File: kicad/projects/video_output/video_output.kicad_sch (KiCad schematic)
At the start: 75 parts, among them J1 peripheral_addr_bus_connector, J10 DATA_BUF_DIR, J11 DATA_BUF_~{OE}, J12 LONG_PULSE, J13 ~{SHORT_PULSE}, J14 GND, J15 SAFE_CLK, J2 peripheral_aux_connector, J3 peripheral_membank_connector, J4 Conn_01x16_Socket, J5 Conn_01x16_Socket, J6 Conn_02x06_Odd_Even, J7 RAM_~{WE}, J8 video_aux, J9 Conn_01x04_Socket, U1 628128_DIP32_SSOP32, U10 74HC157, U11 74HC157, U12 74HC10, U13 74HC02, U14 74HC08, U15 74HC123, U16 74HC32, U17 74HC04, U2 628128_DIP32_SSOP32, U3 74HC245, U4 74HC245, U5 74HC245, U6 74HC245, U7 74HC574, U8 74HC245, U9 74HC574

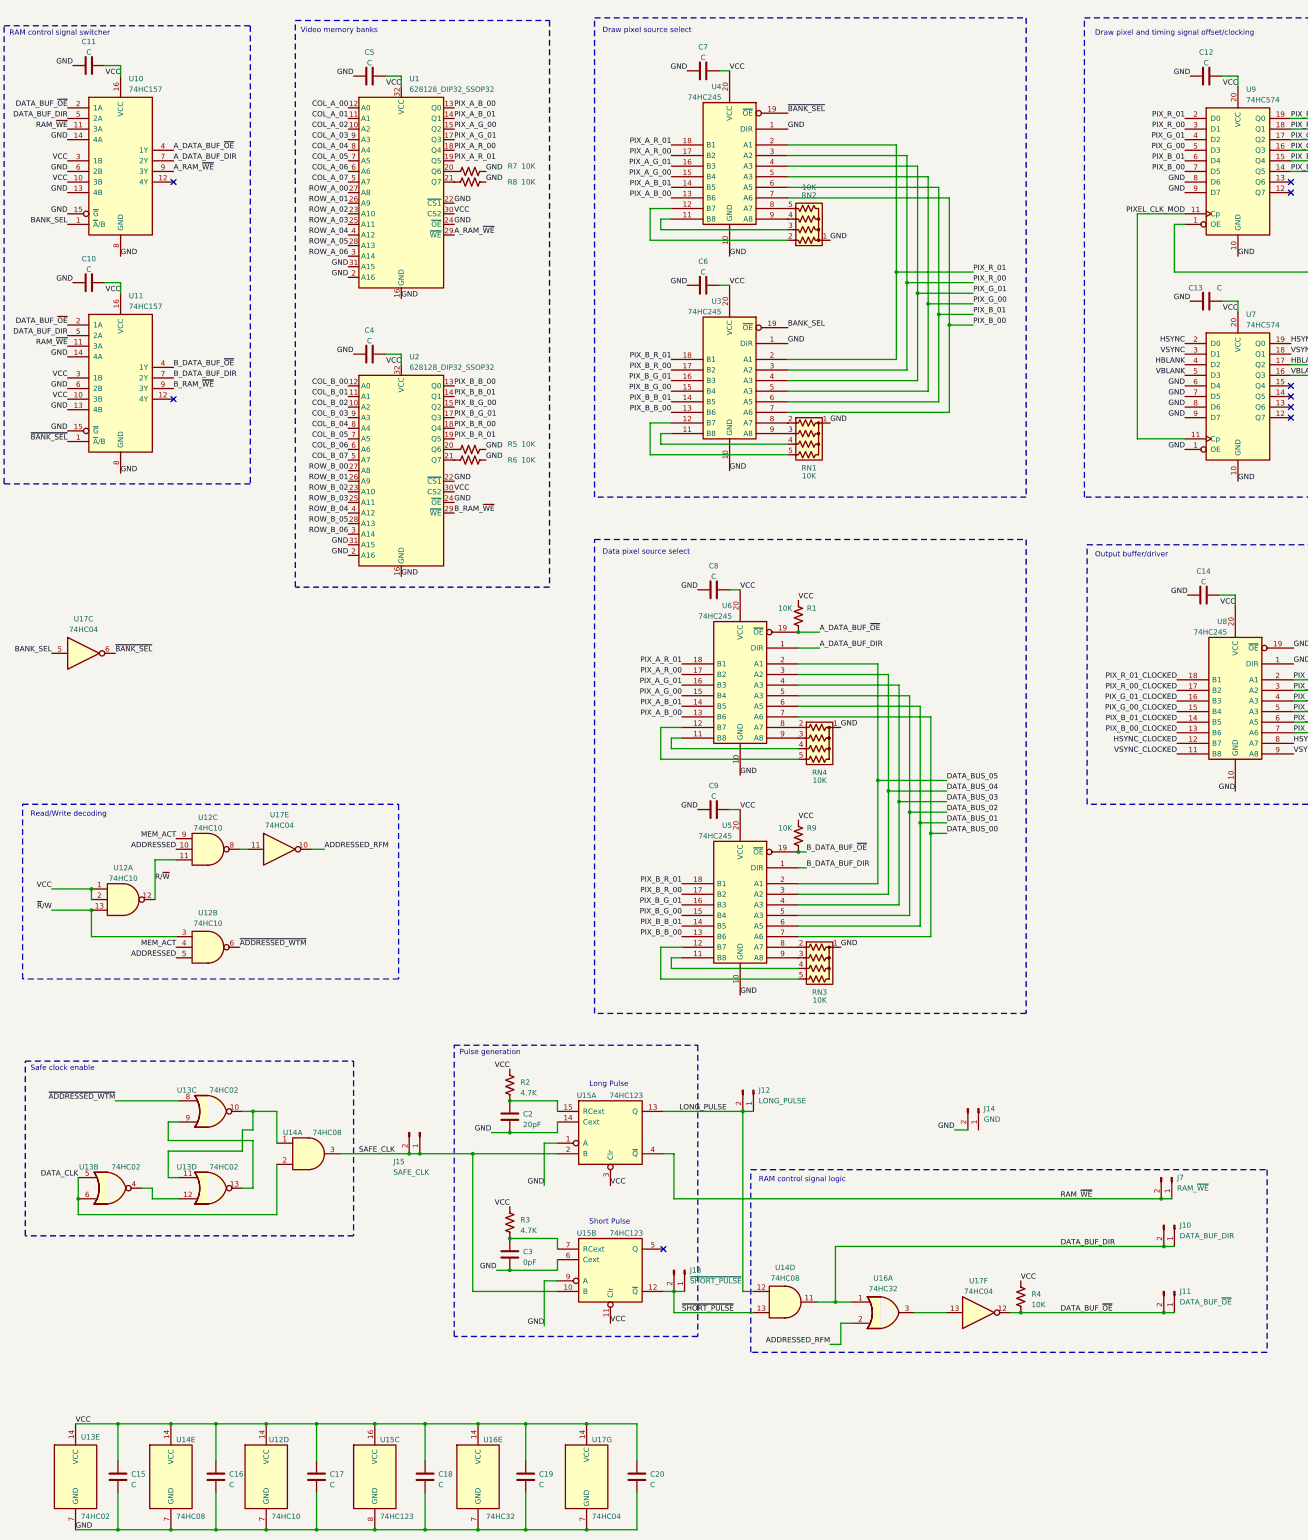
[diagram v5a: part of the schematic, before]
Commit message: Finish updating rom counter to be 32 bit counter
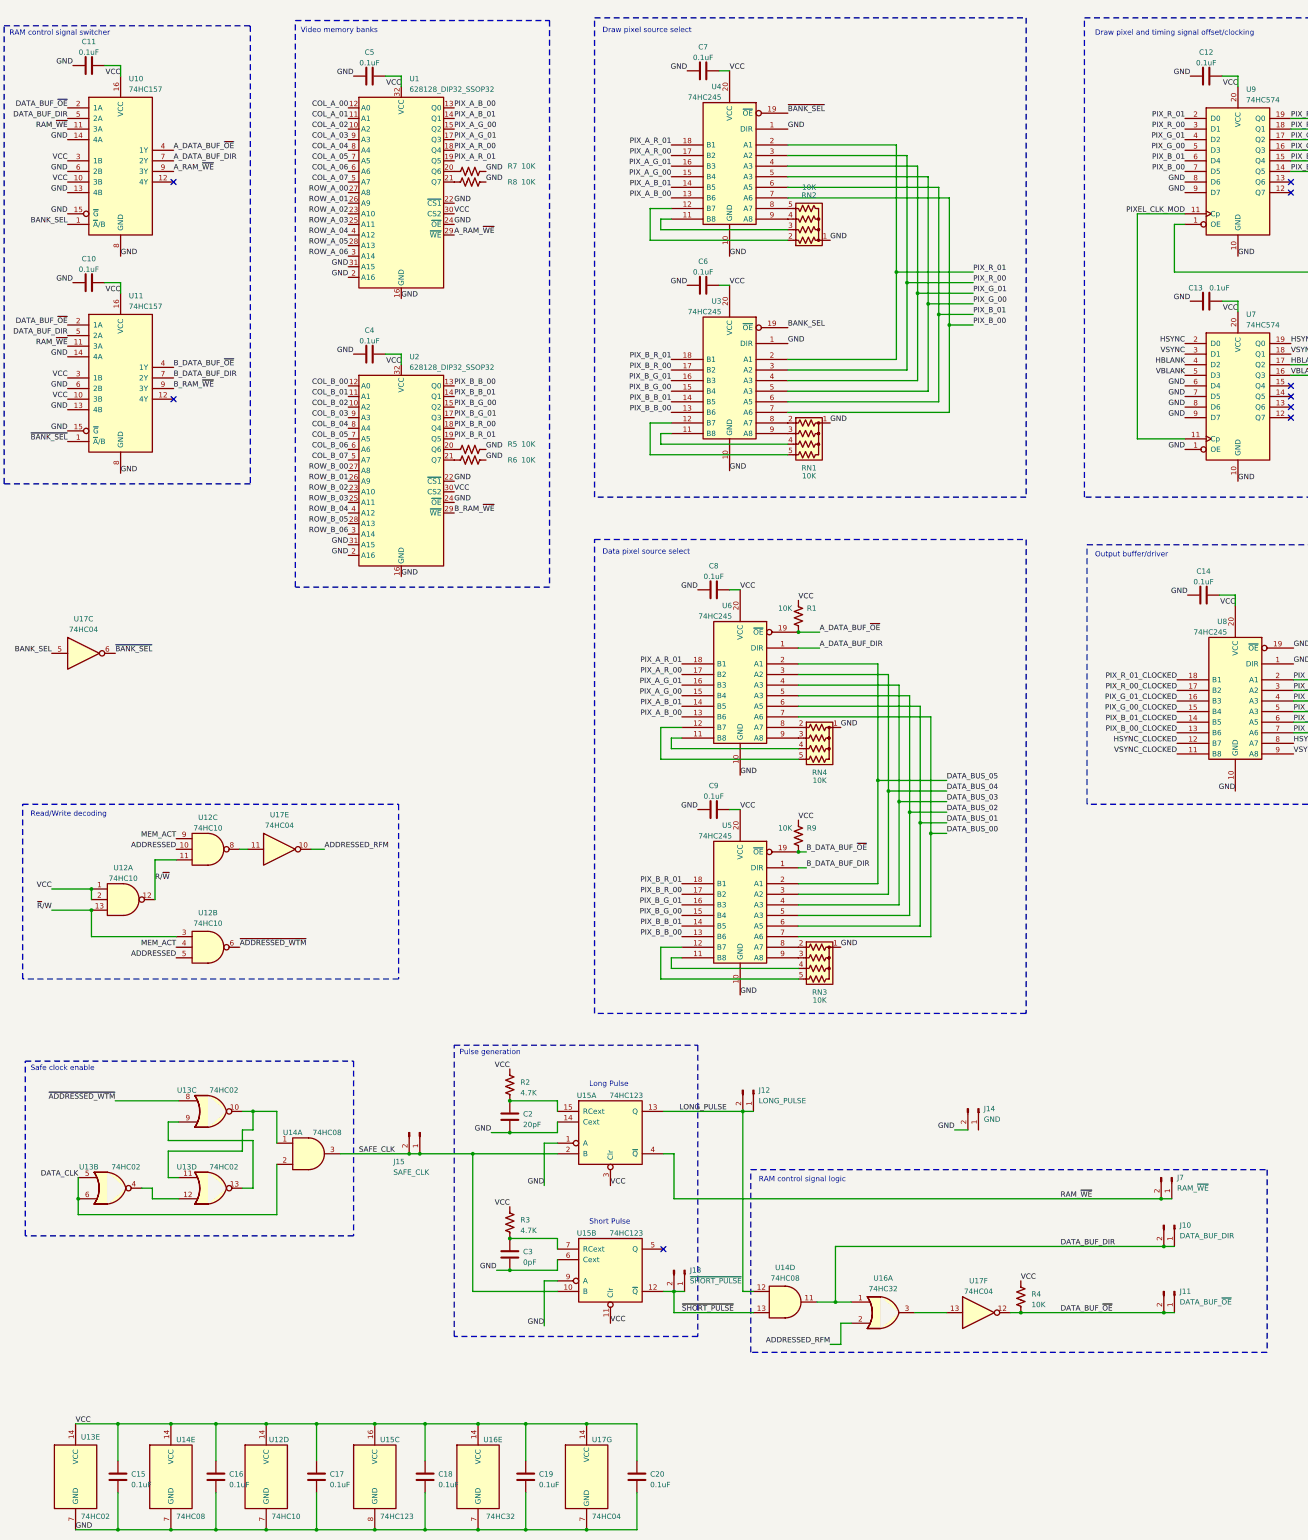
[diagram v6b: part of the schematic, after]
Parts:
- C10, C11, C12, C13, C14, C15, C16, C17, C18, C19, C20, C4, C5, C6, C7, C8, C9: value C -> 0.1uF
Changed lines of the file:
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@@
 (kicad_sch (version 20230121) (generator eeschema)
   (paper "C")
-  (bus_alias "BANK_BUS" (members "BANK_BUS_00" "BANK_BUS_01" "BANK_BUS_02" "BANK_BUS_03" "BANK_BUS_04" "BANK_BUS_05" "BANK_BUS_06" "BANK_BUS_07" "BANK_BUS_08" "BANK_BUS_09" "BANK_BUS_10" "BANK_BUS_11" "BANK_BUS_12" "BANK_BUS_13" "BANK_BUS_14" "BANK_BUS_15"))
   (bus_alias "DATA_BUS" (members "DATA_BUS_00" "DATA_BUS_01" "DATA_BUS_02" "DATA_BUS_03" "DATA_BUS_04" "DATA_BUS_05" "DATA_BUS_06" "DATA_BUS_07" "DATA_BUS_08" "DATA_BUS_09" "DATA_BUS_10" "DATA_BUS_11" "DATA_BUS_12" "DATA_BUS_13" "DATA_BUS_14" "DATA_BUS_15"))
   (bus_alias "ADDR_BUS" (members "ADDR_BUS_00" "ADDR_BUS_01" "ADDR_BUS_02" "ADDR_BUS_03" "ADDR_BUS_04" "ADDR_BUS_05" "ADDR_BUS_06" "ADDR_BUS_07" "ADDR_BUS_08" "ADDR_BUS_09" "ADDR_BUS_10" "ADDR_BUS_11" "ADDR_BUS_12" "ADDR_BUS_13" "ADDR_BUS_14" "ADDR_BUS_15"))
+  (bus_alias "BANK_BUS" (members "BANK_BUS_00" "BANK_BUS_01" "BANK_BUS_02" "BANK_BUS_03" "BANK_BUS_04" "BANK_BUS_05" "BANK_BUS_06" "BANK_BUS_07" "BANK_BUS_08" "BANK_BUS_09" "BANK_BUS_10" "BANK_BUS_11" "BANK_BUS_12" "BANK_BUS_13" "BANK_BUS_14" "BANK_BUS_15"))
   (junction (at 119.38 292.1) (diameter 0) (color 0 0 0 0)
   )
@@
       (effects (font (size 1.27 1.27)))
     )
-    (property "Value" "C" (at 109.855 97.155 90)
+    (property "Value" "0.1uF" (at 109.855 97.155 90)
       (effects (font (size 1.27 1.27)))
     )
@@
       (effects (font (size 1.27 1.27)))
     )
-    (property "Value" "C" (at 192.405 206.375 90)
+    (property "Value" "0.1uF" (at 192.405 206.375 90)
       (effects (font (size 1.27 1.27)))
     )
@@
       (effects (font (size 1.27 1.27)))
     )
-    (property "Value" "C" (at 310.515 30.48 90)
+    (property "Value" "0.1uF" (at 310.515 30.48 90)
       (effects (font (size 1.27 1.27)))
     )
@@
       (effects (font (size 1.27 1.27)) (justify left))
     )
-    (property "Value" "C" (at 177.165 371.475 0)
+    (property "Value" "0.1uF" (at 177.165 371.475 0)
       (effects (font (size 1.27 1.27)) (justify left))
     )
@@
       (effects (font (size 1.27 1.27)))
     )
-    (property "Value" "C" (at 189.865 80.645 90)
+    (property "Value" "0.1uF" (at 189.865 80.645 90)
       (effects (font (size 1.27 1.27)))
     )
@@
       (effects (font (size 1.27 1.27)))
     )
-    (property "Value" "C" (at 192.405 153.67 90)
+    (property "Value" "0.1uF" (at 192.405 153.67 90)
       (effects (font (size 1.27 1.27)))
     )
@@
       (effects (font (size 1.27 1.27)) (justify left))
     )
-    (property "Value" "C" (at 100.33 371.475 0)
+    (property "Value" "0.1uF" (at 100.33 371.475 0)
       (effects (font (size 1.27 1.27)) (justify left))
     )
@@
       (effects (font (size 1.27 1.27)) (justify left))
     )
-    (property "Value" "C" (at 150.495 371.475 0)
+    (property "Value" "0.1uF" (at 150.495 371.475 0)
       (effects (font (size 1.27 1.27)) (justify left))
     )
@@
       (effects (font (size 1.27 1.27)))
     )
-    (property "Value" "C" (at 42.545 80.01 90)
+    (property "Value" "0.1uF" (at 42.545 80.01 90)
       (effects (font (size 1.27 1.27)))
     )
@@
       (effects (font (size 1.27 1.27)))
     )
-    (property "Value" "C" (at 313.69 84.455 90)
+    (property "Value" "0.1uF" (at 313.69 84.455 90)
       (effects (font (size 1.27 1.27)))
     )
@@
       (effects (font (size 1.27 1.27)))
     )
-    (property "Value" "C" (at 309.88 154.94 90)
+    (property "Value" "0.1uF" (at 309.88 154.94 90)
       (effects (font (size 1.27 1.27)))
     )
@@
       (effects (font (size 1.27 1.27)))
     )
-    (property "Value" "C" (at 189.865 29.21 90)
+    (property "Value" "0.1uF" (at 189.865 29.21 90)
       (effects (font (size 1.27 1.27)))
     )
@@
       (effects (font (size 1.27 1.27)))
     )
-    (property "Value" "C" (at 42.545 27.94 90)
+    (property "Value" "0.1uF" (at 42.545 27.94 90)
       (effects (font (size 1.27 1.27)))
     )
@@
       (effects (font (size 1.27 1.27)) (justify left))
     )
-    (property "Value" "C" (at 76.2 371.475 0)
+    (property "Value" "0.1uF" (at 76.2 371.475 0)
       (effects (font (size 1.27 1.27)) (justify left))
     )
@@
       (effects (font (size 1.27 1.27)))
     )
-    (property "Value" "C" (at 109.855 30.48 90)
+    (property "Value" "0.1uF" (at 109.855 30.48 90)
       (effects (font (size 1.27 1.27)))
     )
@@
       (effects (font (size 1.27 1.27)) (justify left))
     )
-    (property "Value" "C" (at 126.365 371.475 0)
+    (property "Value" "0.1uF" (at 126.365 371.475 0)
       (effects (font (size 1.27 1.27)) (justify left))
     )
@@
       (effects (font (size 1.27 1.27)) (justify left))
     )
-    (property "Value" "C" (at 52.705 371.475 0)
+    (property "Value" "0.1uF" (at 52.705 371.475 0)
       (effects (font (size 1.27 1.27)) (justify left))
     )

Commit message: Gerbers generated - order placed
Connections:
- net GND: now also J14.1 (Pin_1)
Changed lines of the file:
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@@
   (junction (at 121.92 292.1) (diameter 0) (color 0 0 0 0)
+  )
+  (junction (at 253.365 286.385) (diameter 0) (color 0 0 0 0)
   )
   (junction (at 123.19 356.87) (diameter 0) (color 0 0 0 0)
@@
     (stroke (width 0) (type default))
   )
+  (wire (pts (xy 253.365 286.385) (xy 255.905 286.385))
+    (stroke (width 0) (type default))
+  )
